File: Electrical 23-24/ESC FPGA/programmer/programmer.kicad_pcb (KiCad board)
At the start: 2 copper layers, 43 parts, among them J1 USB_B_Micro, J2 SFH11-PBPC-D07-ST-BK, J3 Conn_01x05_Pin, J5 Conn_02x8_Pin, J6 Conn_02x8_Pin, SW1 SW_DPST, U1 93C46C, U2 AMS1117-3.3, U3 NUP2202, U4 FT2232HL, X1 ISM92-3351AH-12.000MHZ

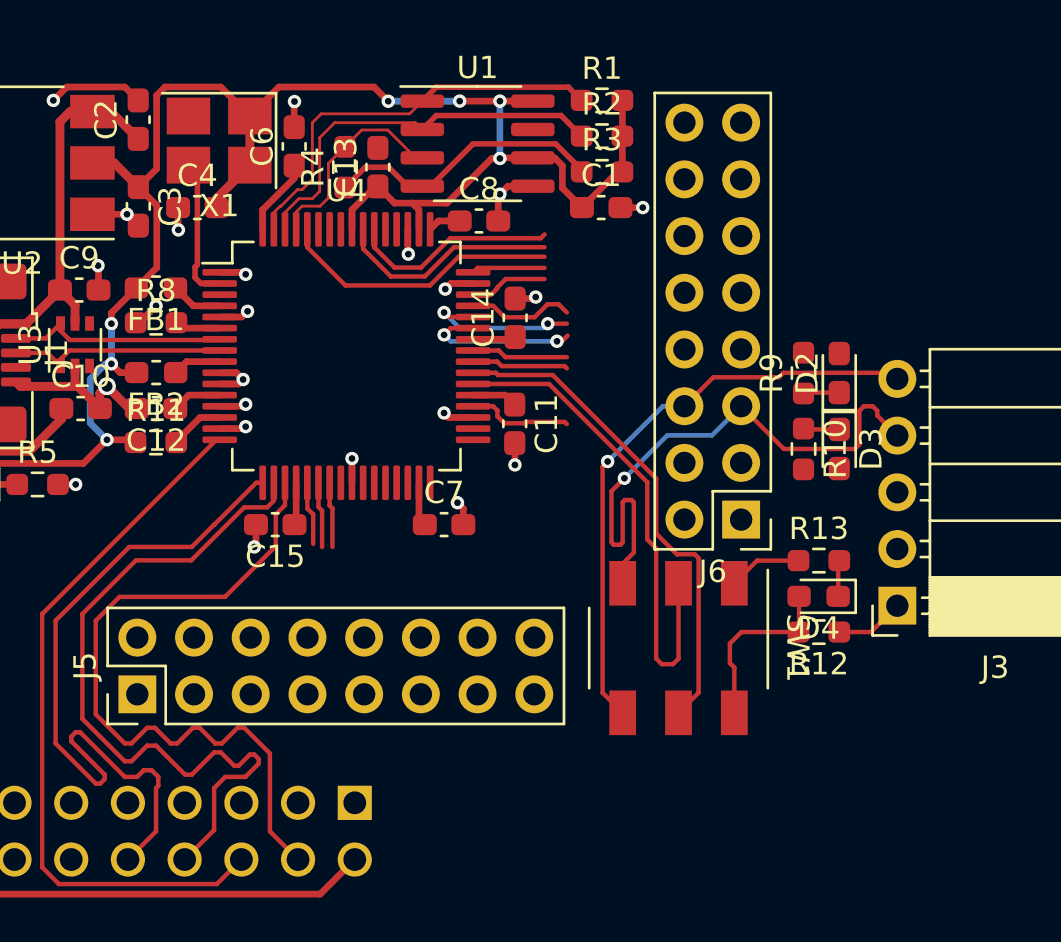
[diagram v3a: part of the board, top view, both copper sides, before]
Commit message: Finished routing, need to add planes
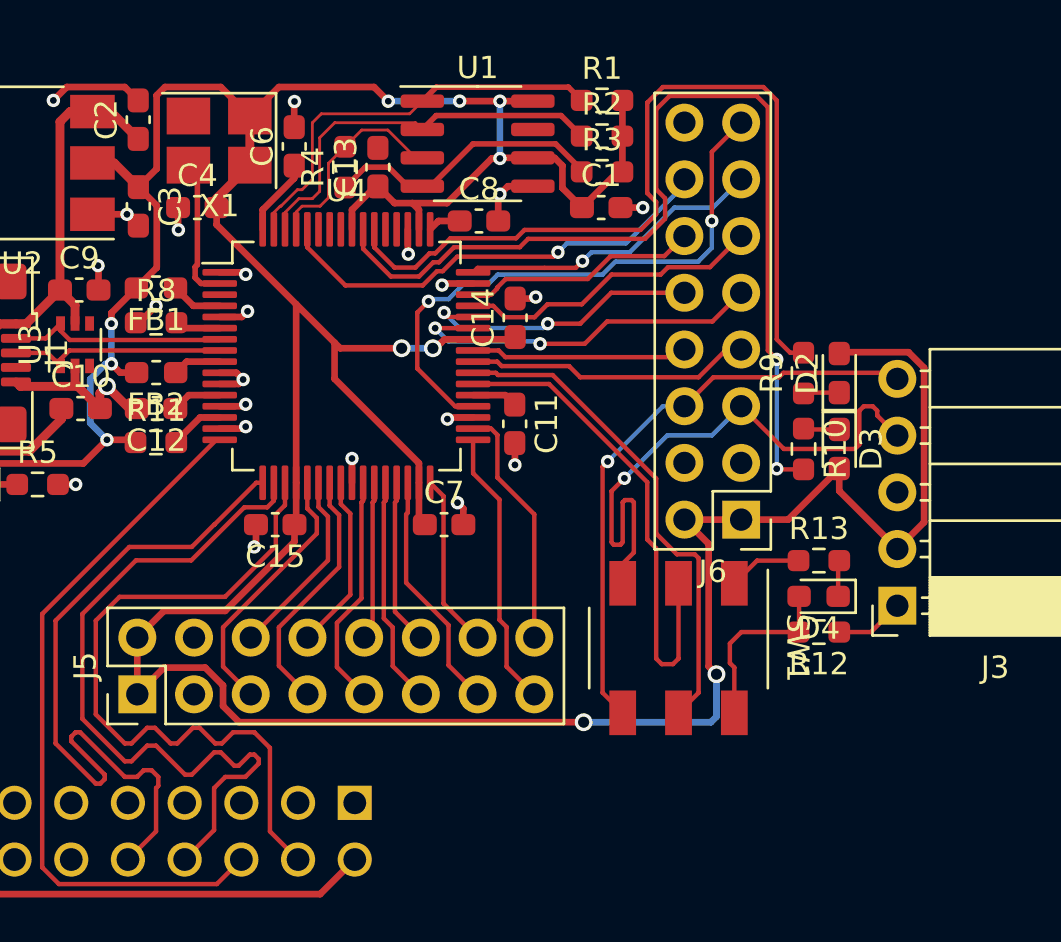
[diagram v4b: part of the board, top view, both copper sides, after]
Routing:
- net +3.3V: track 93.4 -> 199.5 mm, vias 7 -> 11
- net Net-(U4-BCBUS4): track 10.1 -> 44.1 mm, vias 0 -> 2
- net Net-(U4-BCBUS3): track 9.42 -> 38.4 mm
- net /prog/SUS: track 4.73 -> 26.3 mm, vias 0 -> 2
- net /prog/H6: track 0.00 -> 12.5 mm
- net /prog/H7: track 0.00 -> 11.0 mm
- net /prog/H4: track 0.00 -> 10.8 mm
- net /prog/H0: track 0.00 -> 10.5 mm
- net /prog/TXDEN: track 3.28 -> 13.7 mm, vias 0 -> 1
- net /prog/H2: track 0.00 -> 10.2 mm
- net /prog/DTR: track 7.19 -> 16.6 mm
- net /prog/L0: track 2.85 -> 11.9 mm
- net /prog/DCD: track 4.81 -> 13.7 mm
- net /prog/RTS: track 4.32 -> 12.8 mm
- net /prog/L2: track 2.93 -> 11.3 mm
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
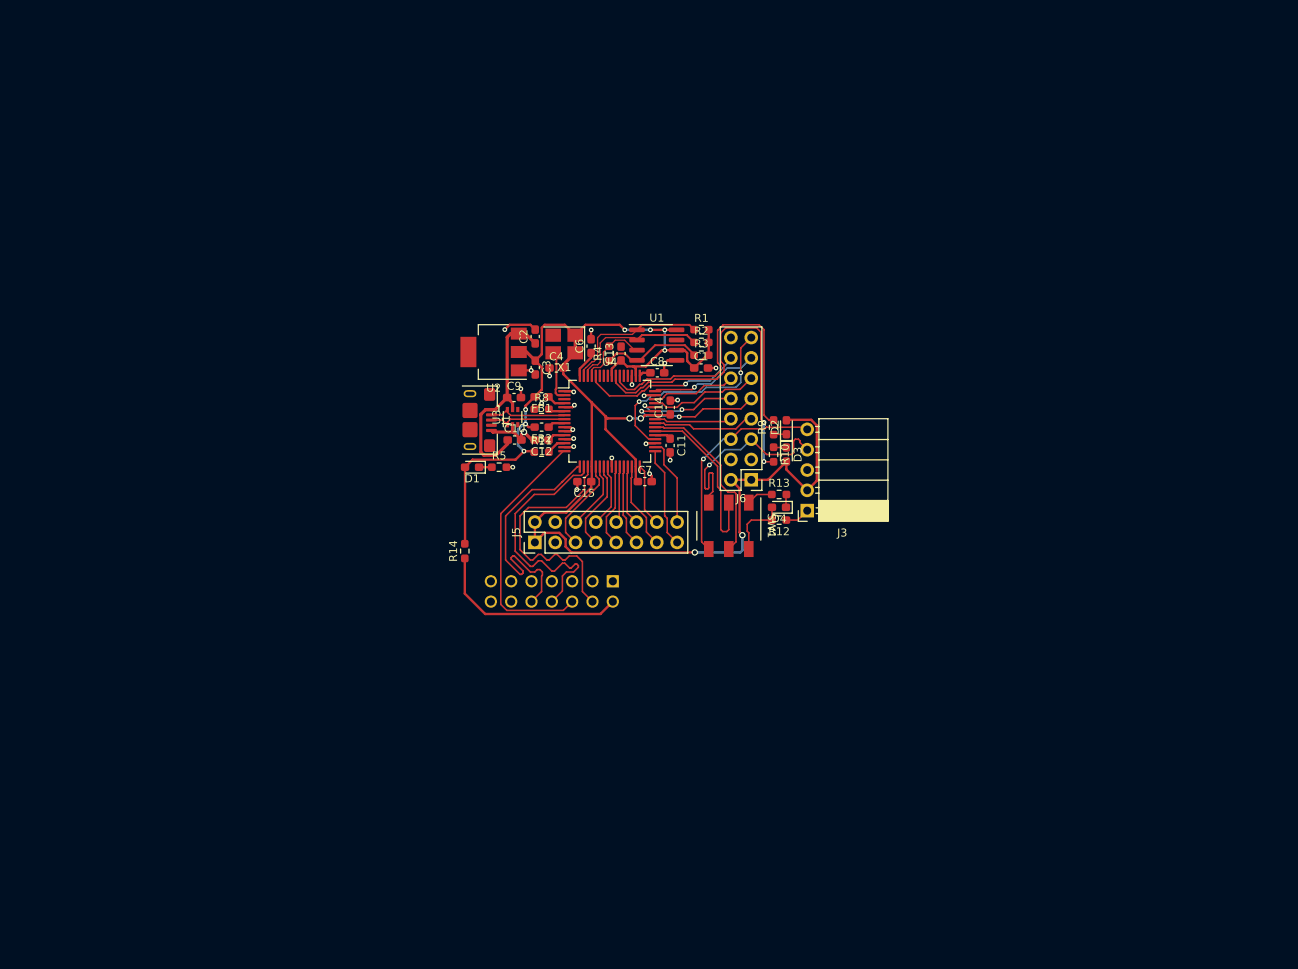
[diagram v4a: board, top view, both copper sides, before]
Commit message: Finished layout, need to DRC
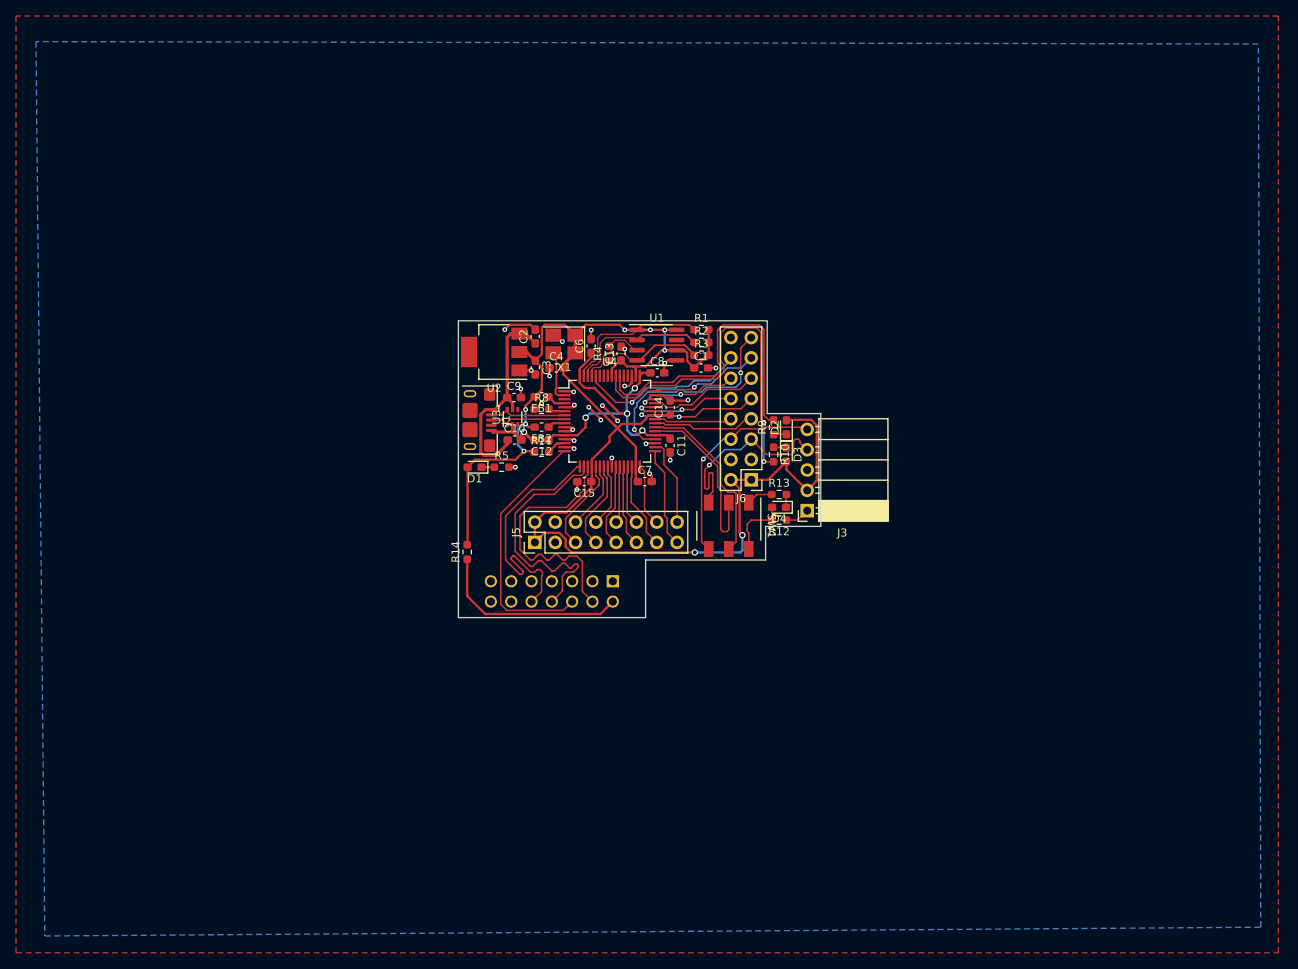
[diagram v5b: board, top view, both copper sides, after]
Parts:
- moved R14 0.32 mm to (98.1, 91.8)
- moved D1 0.32 mm to (99.0, 81.2)
- moved R5 0.32 mm to (102.4, 81.2)
- moved U2 0.07 mm to (101.5, 66.8)
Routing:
- net +1V8: track 9.19 -> 39.0 mm, vias 0 -> 4
- net GND: track 39.9 -> 49.9 mm, vias 23 -> 28
- net /prog/RI: track 10.6 -> 13.4 mm, vias 0 -> 2
- net +3.3V: track 199.5 -> 196.9 mm, vias 11 -> 9
- net Net-(U4-BCBUS4): track 44.1 -> 45.1 mm
- net Net-(U4-BCBUS3): track 38.4 -> 39.5 mm
- net /prog/PWREN: track 20.5 -> 21.3 mm
- net /prog/SUS: track 26.3 -> 27.0 mm
- net /prog/DSR: track 13.1 -> 13.7 mm
- added copper zone on B.Cu, net GND
- added copper zone on F.Cu, net GND
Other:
- board outline added: 45.3 x 37.1 mm

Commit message: Finished board
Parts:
- moved D1 1.13 mm to (99.0, 82.3)
- moved R5 1.13 mm to (102.4, 82.3)
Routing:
- net +3.3V: track 196.9 -> 198.0 mm
- net GND: track 49.9 -> 50.8 mm
- removed copper zone on F.Cu, net GND
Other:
- outline, holes or cut-outs redrawn
- board text added: "3V3"
- board text added: "3V3 REG"
- board text added: "ADV UART"
- board text added: "CTS"
- board text added: "DCD"
- board text added: "DSR"
- board text added: "DTR"
- board text added: "FLASH"
- board text added: "FTDI-2232"
- board text added: "GND"
- board text added: "H0"
- board text added: "H1"
- board text added: "H2"
- board text added: "H3"
- board text added: "H4"
- board text added: "H5"
- board text added: "H6"
- board text added: "H7"
- board text added: "JTAG/UART Programmer V1 Ari Bobesh 04/07/2024"
- board text added: "L0"
- board text added: "L1"
- board text added: "L2"
- board text added: "L3"
- board text added: "OSCI"
- board text added: "PEN"
- board text added: "PMOD/GPIO"
- board text added: "POWER"
- board text added: "REF"
- board text added: "RI"
- board text added: "RTS"
- board text added: "RX"
- board text added: "SUS"
- board text added: "SWITCH"
- board text added: "TCK"
- board text added: "TDI"
- board text added: "TDO"
- board text added: "TEN"
- board text added: "TMS"
- board text added: "TX"
- board text added: "UART UPDI"
- board text added: "UART<->UPDI"
- board text added: "UPDI"
- board text added: "UPDI <-> UART"
- board text added: "USB uB"
- board text added: "XILINX JTAG"

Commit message: Add JLC Serial # Location to All
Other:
- board text added: "JLCJLCJLCJLC"
